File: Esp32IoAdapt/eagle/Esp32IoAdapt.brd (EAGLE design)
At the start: 11.4 x 39.7 mm, 9 parts

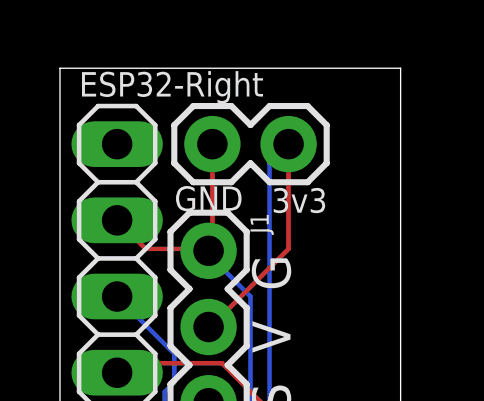
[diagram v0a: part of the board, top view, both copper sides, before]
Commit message: Corrected left vs right nomenclature
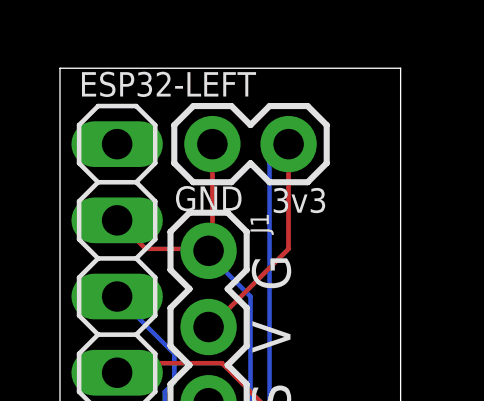
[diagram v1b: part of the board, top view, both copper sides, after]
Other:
- board text added: "ESP32-LEFT"
- board text removed: "ESP32-Right"
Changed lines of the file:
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@@
 <?xml version="1.0" encoding="utf-8"?>
 <!DOCTYPE eagle SYSTEM "eagle.dtd">
-<eagle version="9.5.2">
+<eagle version="9.6.2">
 <drawing>
 <settings>
@@
 <text x="8.3185" y="68.5165" size="1.27" layer="25" rot="R90">S  V  G</text>
 <text x="9.398" y="74.803" size="1.778" layer="26" rot="MR270">ESP32 I/O Adapt v1.0</text>
-<text x="1.27" y="79.0575" size="0.8128" layer="25">ESP32-Right</text>
+<text x="1.27" y="79.0575" size="0.8128" layer="25">ESP32-LEFT</text>
 </plain>
 <attributes>
